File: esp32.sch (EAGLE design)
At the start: 52 parts, among them IC1 PEC11R-4230K-S00243D, IC2 AD8532ARZ, T1 BST82-1, T2 BST82-1, U1 ESP32-WROOM-32D, X1 JST-XH-02-PIN-LONG-PAD, X2 JST-XH-03-PIN-LONG-PAD, X3 JST-XH-03-PIN-LONG-PAD, X4 JST-XH-02-PIN-LONG-PAD

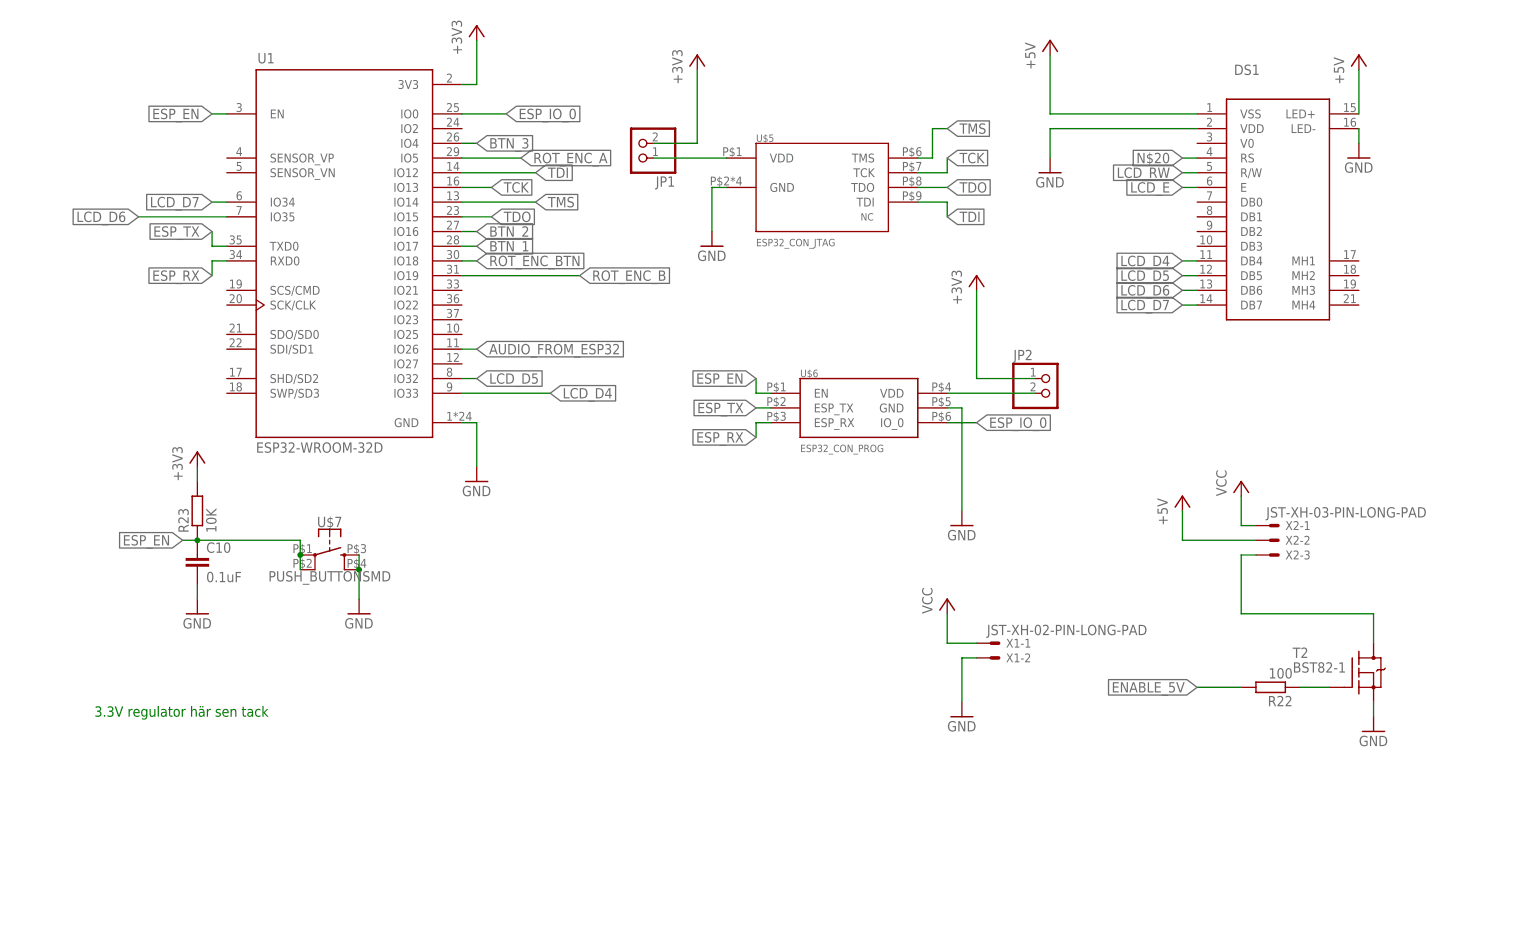
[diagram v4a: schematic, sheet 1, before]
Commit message: La till kondingar och kopplade alla signaler, precis lagom många GPIO pinnar på ESP32an typ bara 2 över!
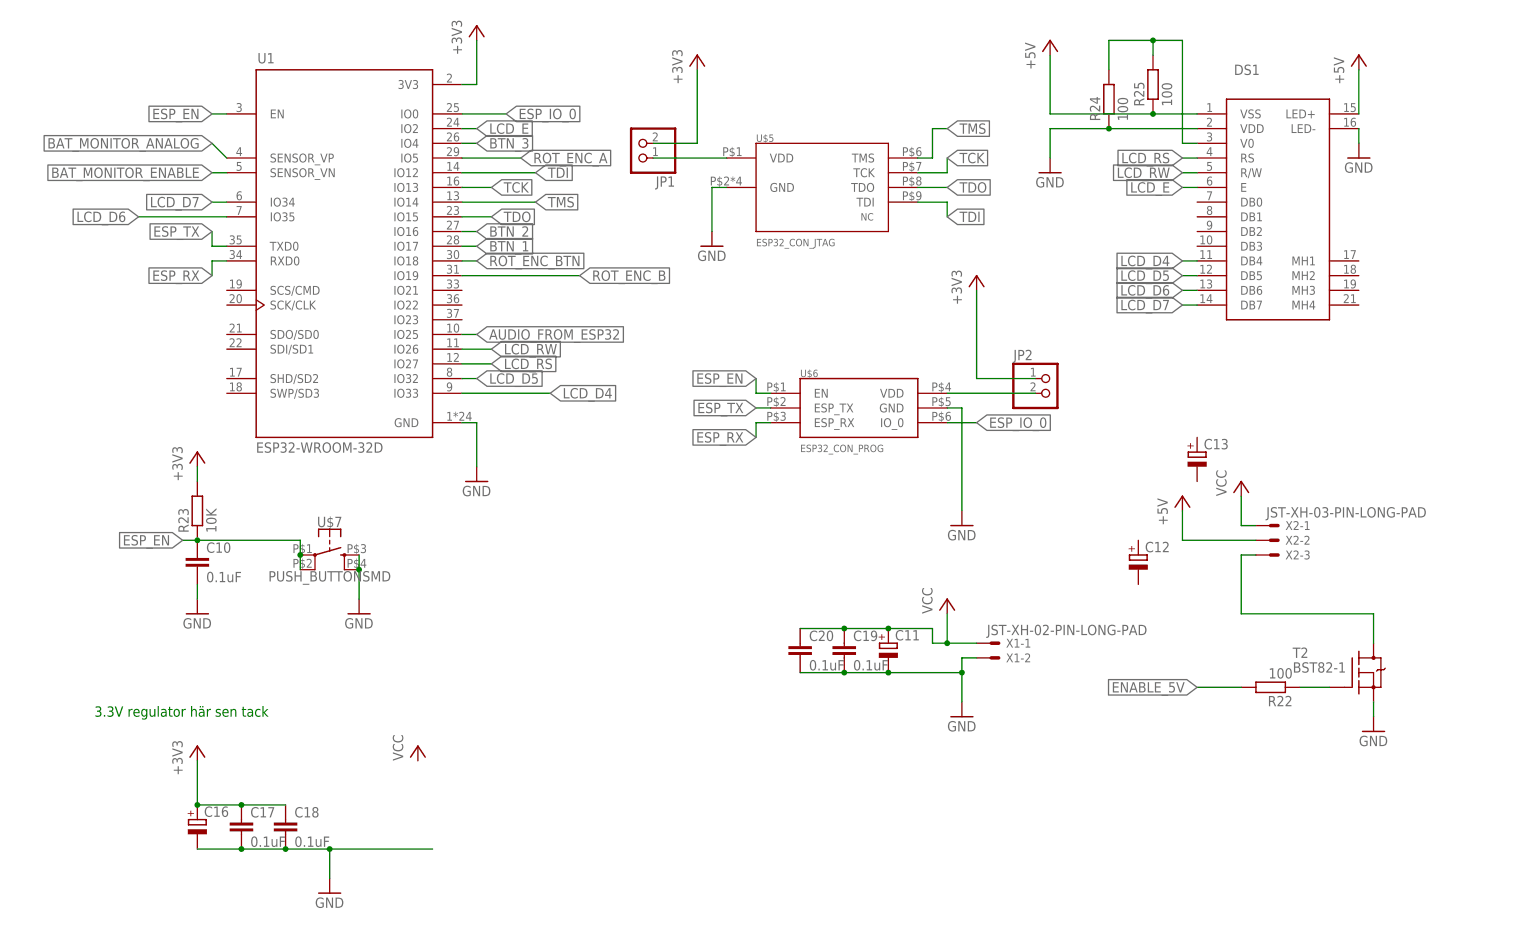
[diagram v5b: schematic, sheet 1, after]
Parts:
- added C11, C12, C13, C16, C22: (no value), rcl:CPOL-EU140CLH-0810
- added C14: 270uF, rcl:CPOL-EU140CLH-0810
- added C17, C18, C19, C20: 0.1uF, rcl:C-EUC0603
- added C21: 10uF, rcl:C-EUC0603
- added R24, R25: 100, rcl:R-EU_R0603
- C9: value 270uF -> 10uF
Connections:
- removed net N$20: DS1.RS
- new net LCD_RS: DS1.RS, U1.IO27
- new net N$17: DS1.V0, R24.2, R25.2
- net +3V3: now also C16.+, C17.1, C18.1
- net +5V: now also C21.1, C22.+, C9.1, R25.1
- net AUDIO_FROM_ESP32: now also U1.IO25; no longer U1.IO26
- net BAT_MONITOR_ANALOG: now also U1.SENSOR_VP
- net BAT_MONITOR_ENABLE: now also U1.SENSOR_VN
- net GND: now also C11.-, C16.-, C17.2, C18.2, C19.2, C20.2, C21.2, C22.-, C9.2, R24.1
- net LCD_E: now also U1.IO2
- net LCD_RW: now also U1.IO26
- net N$14: now also C14.+; no longer C9.1
- net SPEAKER_OUT: now also C14.-; no longer C9.2
- net VCC: now also C11.+, C19.1, C20.1
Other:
- moved on the sheet: C9

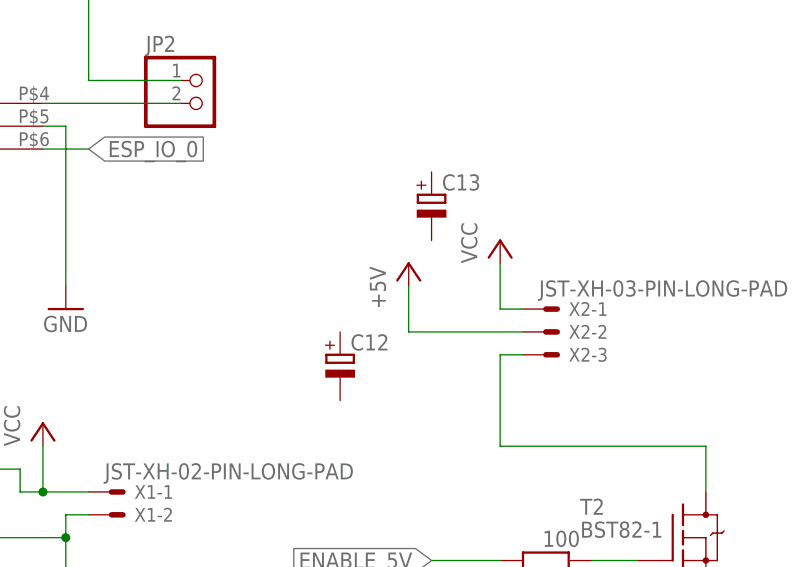
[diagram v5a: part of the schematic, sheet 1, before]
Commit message: Fixade så att texten har orphans i fyllkomandot, såg konstigt ut annars.
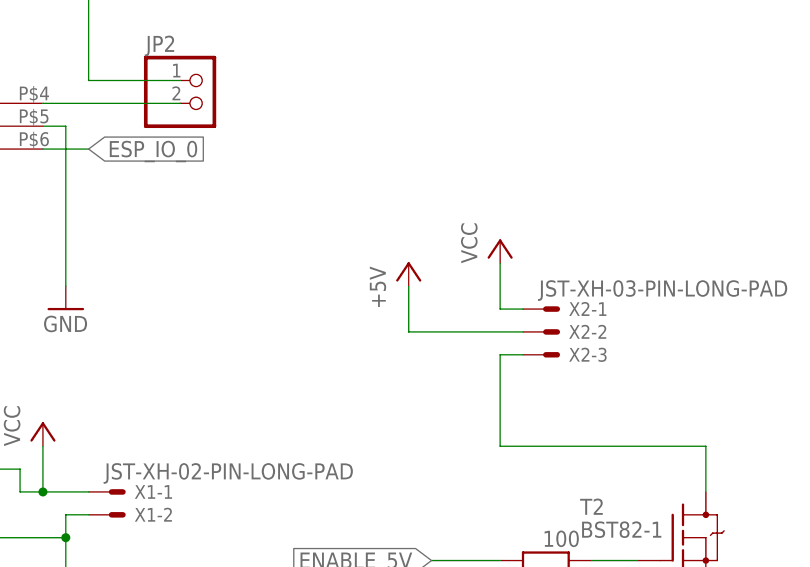
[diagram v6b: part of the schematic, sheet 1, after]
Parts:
- removed C12, C13: (no value), rcl:CPOL-EU140CLH-0810
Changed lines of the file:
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@@
 <grid distance="0.1" unitdist="inch" unit="inch" style="lines" multiple="1" display="no" altdistance="0.01" altunitdist="inch" altunit="inch"/>
 <layers>
-<layer number="1" name="Top" color="4" fill="1" visible="yes" active="no"/>
-<layer number="2" name="Route2" color="16" fill="1" visible="yes" active="no"/>
-<layer number="3" name="Route3" color="17" fill="1" visible="yes" active="no"/>
-<layer number="4" name="Route4" color="18" fill="1" visible="yes" active="no"/>
-<layer number="5" name="Route5" color="19" fill="1" visible="yes" active="no"/>
-<layer number="6" name="Route6" color="25" fill="1" visible="yes" active="no"/>
-<layer number="7" name="Route7" color="26" fill="1" visible="yes" active="no"/>
-<layer number="8" name="Route8" color="27" fill="1" visible="yes" active="no"/>
-<layer number="9" name="Route9" color="28" fill="1" visible="yes" active="no"/>
-<layer number="10" name="Route10" color="29" fill="1" visible="yes" active="no"/>
-<layer number="11" name="Route11" color="30" fill="1" visible="yes" active="no"/>
-<layer number="12" name="Route12" color="20" fill="1" visible="yes" active="no"/>
-<layer number="13" name="Route13" color="21" fill="1" visible="yes" active="no"/>
-<layer number="14" name="Route14" color="22" fill="1" visible="yes" active="no"/>
-<layer number="15" name="Route15" color="23" fill="1" visible="yes" active="no"/>
-<layer number="16" name="Bottom" color="1" fill="1" visible="yes" active="no"/>
-<layer number="17" name="Pads" color="2" fill="1" visible="yes" active="no"/>
-<layer number="18" name="Vias" color="2" fill="1" visible="yes" active="no"/>
-<layer number="19" name="Unrouted" color="6" fill="1" visible="yes" active="no"/>
-<layer number="20" name="Dimension" color="24" fill="1" visible="yes" active="no"/>
-<layer number="21" name="tPlace" color="7" fill="1" visible="yes" active="no"/>
-<layer number="22" name="bPlace" color="7" fill="1" visible="yes" active="no"/>
-<layer number="23" name="tOrigins" color="15" fill="1" visible="yes" active="no"/>
-<layer number="24" name="bOrigins" color="15" fill="1" visible="yes" active="no"/>
-<layer number="25" name="tNames" color="7" fill="1" visible="yes" active="no"/>
-<layer number="26" name="bNames" color="7" fill="1" visible="yes" active="no"/>
-<layer number="27" name="tValues" color="7" fill="1" visible="yes" active="no"/>
-<layer number="28" name="bValues" color="7" fill="1" visible="yes" active="no"/>
+<layer number="1" name="Top" color="4" fill="1" visible="no" active="no"/>
+<layer number="2" name="Route2" color="16" fill="1" visible="no" active="no"/>
+<layer number="3" name="Route3" color="17" fill="1" visible="no" active="no"/>
+<layer number="4" name="Route4" color="18" fill="1" visible="no" active="no"/>
+<layer number="5" name="Route5" color="19" fill="1" visible="no" active="no"/>
+<layer number="6" name="Route6" color="25" fill="1" visible="no" active="no"/>
+<layer number="7" name="Route7" color="26" fill="1" visible="no" active="no"/>
+<layer number="8" name="Route8" color="27" fill="1" visible="no" active="no"/>
+<layer number="9" name="Route9" color="28" fill="1" visible="no" active="no"/>
+<layer number="10" name="Route10" color="29" fill="1" visible="no" active="no"/>
+<layer number="11" name="Route11" color="30" fill="1" visible="no" active="no"/>
+<layer number="12" name="Route12" color="20" fill="1" visible="no" active="no"/>
+<layer number="13" name="Route13" color="21" fill="1" visible="no" active="no"/>
+<layer number="14" name="Route14" color="22" fill="1" visible="no" active="no"/>
+<layer number="15" name="Route15" color="23" fill="1" visible="no" active="no"/>
+<layer number="16" name="Bottom" color="1" fill="1" visible="no" active="no"/>
+<layer number="17" name="Pads" color="2" fill="1" visible="no" active="no"/>
+<layer number="18" name="Vias" color="2" fill="1" visible="no" active="no"/>
+<layer number="19" name="Unrouted" color="6" fill="1" visible="no" active="no"/>
+<layer number="20" name="Dimension" color="24" fill="1" visible="no" active="no"/>
+<layer number="21" name="tPlace" color="7" fill="1" visible="no" active="no"/>
+<layer number="22" name="bPlace" color="7" fill="1" visible="no" active="no"/>
+<layer number="23" name="tOrigins" color="15" fill="1" visible="no" active="no"/>
+<layer number="24" name="bOrigins" color="15" fill="1" visible="no" active="no"/>
+<layer number="25" name="tNames" color="7" fill="1" visible="no" active="no"/>
+<layer number="26" name="bNames" color="7" fill="1" visible="no" active="no"/>
+<layer number="27" name="tValues" color="7" fill="1" visible="no" active="no"/>
+<layer number="28" name="bValues" color="7" fill="1" visible="no" active="no"/>
 <layer number="29" name="tStop" color="7" fill="3" visible="no" active="no"/>
 <layer number="30" name="bStop" color="7" fill="6" visible="no" active="no"/>
@@
 <layer number="35" name="tGlue" color="7" fill="4" visible="no" active="no"/>
 <layer number="36" name="bGlue" color="7" fill="5" visible="no" active="no"/>
-<layer number="37" name="tTest" color="7" fill="1" visible="yes" active="no"/>
-<layer number="38" name="bTest" color="7" fill="1" visible="yes" active="no"/>
+<layer number="37" name="tTest" color="7" fill="1" visible="no" active="no"/>
+<layer number="38" name="bTest" color="7" fill="1" visible="no" active="no"/>
 <layer number="39" name="tKeepout" color="4" fill="11" visible="no" active="no"/>
 <layer number="40" name="bKeepout" color="1" fill="11" visible="no" active="no"/>
@@
 <layer number="44" name="Drills" color="7" fill="1" visible="no" active="no"/>
 <layer number="45" name="Holes" color="7" fill="1" visible="no" active="no"/>
-<layer number="46" name="Milling" color="3" fill="1" visible="yes" active="no"/>
-<layer number="47" name="Measures" color="7" fill="1" visible="yes" active="no"/>
-<layer number="48" name="Document" color="7" fill="1" visible="yes" active="no"/>
-<layer number="49" name="Reference" color="7" fill="1" visible="yes" active="no"/>
-<layer number="50" name="dxf" color="7" fill="1" visible="yes" active="no"/>
-<layer number="51" name="tDocu" color="7" fill="1" visible="yes" active="no"/>
-<layer number="52" name="bDocu" color="7" fill="1" visible="yes" active="no"/>
-<layer number="53" name="tGND_GNDA" color="7" fill="9" visible="yes" active="no"/>
-<layer number="54" name="bGND_GNDA" color="1" fill="9" visible="yes" active="no"/>
-<layer number="56" name="wert" color="7" fill="1" visible="yes" active="no"/>
-<layer number="57" name="tCAD" color="7" fill="1" visible="yes" active="no"/>
-<layer number="59" name="tCarbon" color="7" fill="1" visible="yes" active="no"/>
-<layer number="60" name="bCarbon" color="7" fill="1" visible="yes" active="no"/>
+<layer number="46" name="Milling" color="3" fill="1" visible="no" active="no"/>
+<layer number="47" name="Measures" color="7" fill="1" visible="no" active="no"/>
+<layer number="48" name="Document" color="7" fill="1" visible="no" active="no"/>
+<layer number="49" name="Reference" color="7" fill="1" visible="no" active="no"/>
+<layer number="50" name="dxf" color="7" fill="1" visible="no" active="no"/>
+<layer number="51" name="tDocu" color="7" fill="1" visible="no" active="no"/>
+<layer number="52" name="bDocu" color="7" fill="1" visible="no" active="no"/>
+<layer number="53" name="tGND_GNDA" color="7" fill="9" visible="no" active="no"/>
+<layer number="54" name="bGND_GNDA" color="1" fill="9" visible="no" active="no"/>
+<layer number="56" name="wert" color="7" fill="1" visible="no" active="no"/>
+<layer number="57" name="tCAD" color="7" fill="1" visible="no" active="no"/>
+<layer number="59" name="tCarbon" color="7" fill="1" visible="no" active="no"/>
+<layer number="60" name="bCarbon" color="7" fill="1" visible="no" active="no"/>
 <layer number="88" name="SimResults" color="9" fill="1" visible="yes" active="yes"/>
 <layer number="89" name="SimProbes" color="9" fill="1" visible="yes" active="yes"/>
@@
 <part name="GND24" library="supply1" library_urn="urn:adsk.eagle:library:371" deviceset="GND" device=""/>
 <part name="C11" library="rcl" library_urn="urn:adsk.eagle:library:334" deviceset="CPOL-EU" device="140CLH-0810" package3d_urn="urn:adsk.eagle:package:23392/2"/>
-<part name="C12" library="rcl" library_urn="urn:adsk.eagle:library:334" deviceset="CPOL-EU" device="140CLH-0810" package3d_urn="urn:adsk.eagle:package:23392/2"/>
-<part name="C13" library="rcl" library_urn="urn:adsk.eagle:library:334" deviceset="CPOL-EU" device="140CLH-0810" package3d_urn="urn:adsk.eagle:package:23392/2"/>
 <part name="C14" library="rcl" library_urn="urn:adsk.eagle:library:334" deviceset="CPOL-EU" device="140CLH-0810" package3d_urn="urn:adsk.eagle:package:23392/2" value="270uF"/>
 <part name="C16" library="rcl" library_urn="urn:adsk.eagle:library:334" deviceset="CPOL-EU" device="140CLH-0810" package3d_urn="urn:adsk.eagle:package:23392/2"/>
@@
 <attribute name="VALUE" x="156.083" y="48.7426" size="1.778" layer="96"/>
 </instance>
-<instance part="C12" gate="G$1" x="198.12" y="68.58" smashed="yes">
-<attribute name="NAME" x="199.263" y="69.0626" size="1.778" layer="95"/>
-<attribute name="VALUE" x="199.263" y="63.9826" size="1.778" layer="96"/>
-</instance>
-<instance part="C13" gate="G$1" x="208.28" y="86.36" smashed="yes">
-<attribute name="NAME" x="209.423" y="86.8426" size="1.778" layer="95"/>
-<attribute name="VALUE" x="209.423" y="81.7626" size="1.778" layer="96"/>
-</instance>
 <instance part="C16" gate="G$1" x="35.56" y="22.86" smashed="yes">
